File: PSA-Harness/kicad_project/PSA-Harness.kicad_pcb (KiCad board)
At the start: 2 copper layers, 32 x 50 mm, 11 parts, among them J1 to_EPS_1, J2 to_EPS_2, J3 to_ESP_3, J4 to_car_1, J5 to_car_2, J6 to_car_3, J7 USB_C_Receptacle, K1 G6K-2G-Y DC5

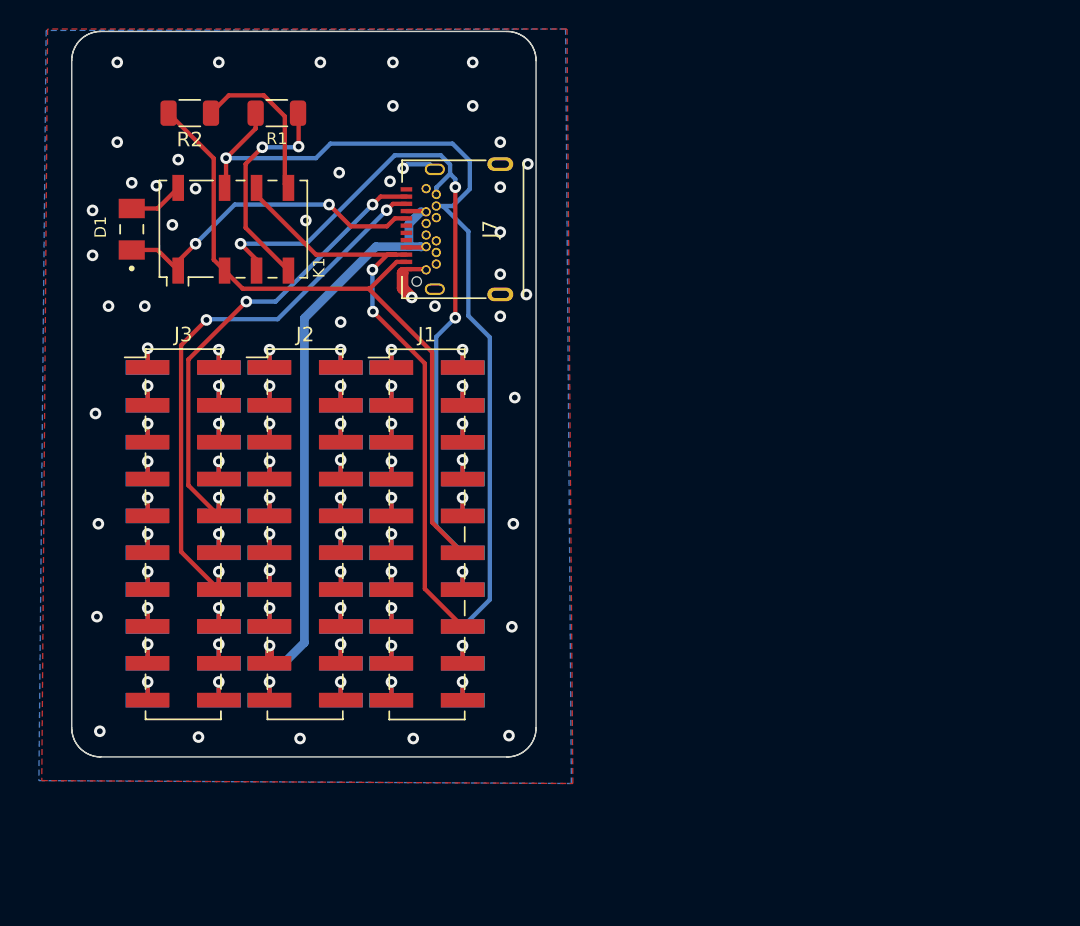
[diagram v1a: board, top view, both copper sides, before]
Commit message: chg: use correct footprints, SMD socket clearence too low
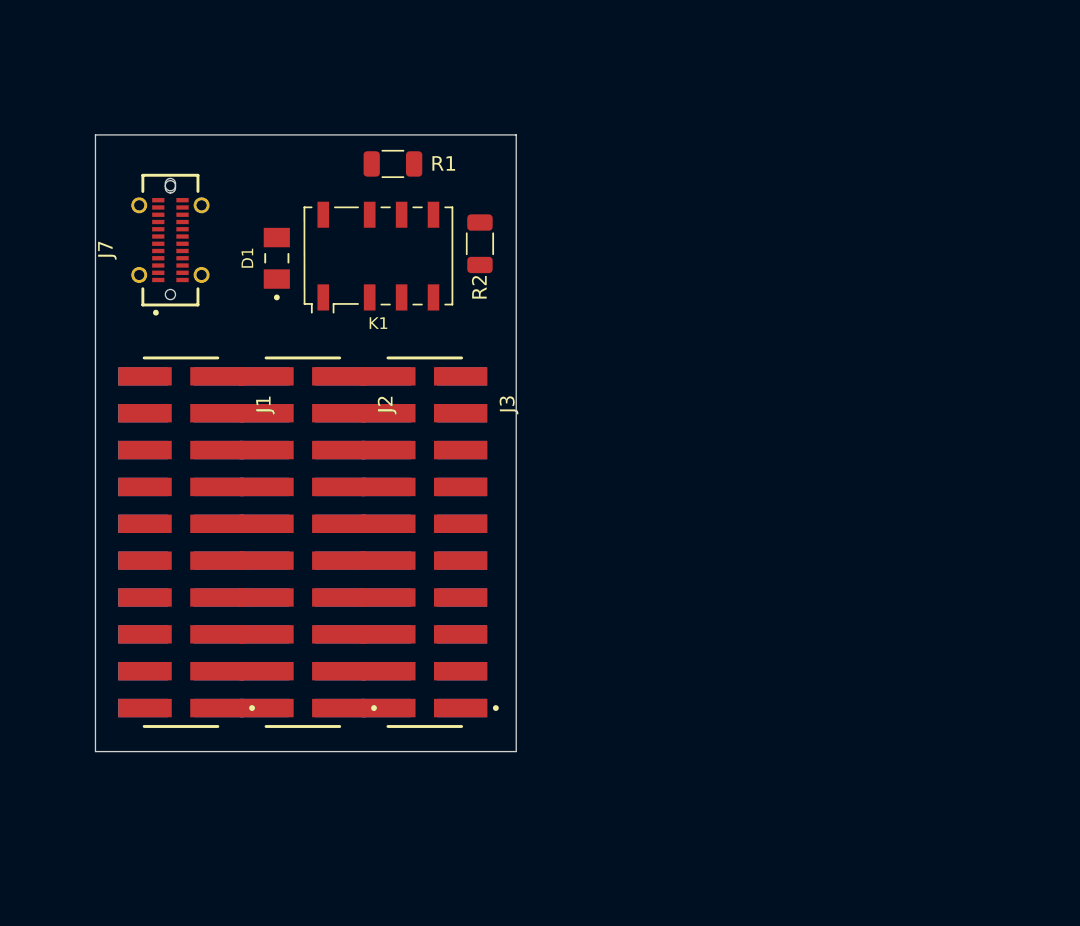
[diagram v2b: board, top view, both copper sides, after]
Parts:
- J1, J2, J3: footprint PSA:PinHeader_2x10_P2.54mm_Vertical_SMD_PSA_small -> PSA:TSM-110-03-X-DV
- J4, J5, J6: footprint PSA:PinSocket_2x10_P2.54mm_Vertical_SMD_PSA -> PSA:SSW-110-22-F-D-VS-K-TR
- J7: footprint PSA:TYPE-C-31-M-04 -> PSA:GCT_USB4115-03-C_REVB4
- moved R2 21.9 mm to (118.0, 101.0), turned to -90 degrees
- moved J7 21.3 mm to (96.7, 100.8)
- moved J4 17.0 mm to (97.4, 121.6), turned to -90 degrees
- moved J1 17.0 mm to (97.4, 121.6), turned to -90 degrees
- moved J3 16.7 mm to (114.2, 121.6), turned to -90 degrees
- moved J6 16.6 mm to (114.2, 121.6), turned to -90 degrees
- moved D1 10.2 mm to (104.0, 102.0)
- moved K1 10.2 mm to (111.0, 101.8)
- moved R1 8.73 mm to (112.0, 95.5)
- moved J5 0.57 mm to (105.8, 121.6), turned to -90 degrees
- moved J2 0.57 mm to (105.8, 121.6), turned to -90 degrees
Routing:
- net CAN2_L: track 59.6 -> 0.00 mm, vias 1 -> 0
- net CAN2_H: track 49.6 -> 0.00 mm, vias 3 -> 0
- net CAN0_H: track 47.1 -> 0.00 mm
- net +12V: track 43.5 -> 0.00 mm, vias 1 -> 0
- net CAN0_L: track 41.7 -> 0.00 mm, vias 2 -> 0
- net CAN1_L: track 40.0 -> 0.00 mm, vias 3 -> 0
- net CAN1_H: track 33.8 -> 0.00 mm, vias 3 -> 0
- net SBU1: track 22.6 -> 0.00 mm, vias 2 -> 0
- net Relay_4: track 15.0 -> 0.00 mm, vias 2 -> 0
- net GND: track 12.1 -> 0.00 mm, vias 43 -> 0
- net Relay_5: track 11.2 -> 0.00 mm
- net 9: track 2.69 -> 0.00 mm, vias 1 -> 0
- net 19: track 2.69 -> 0.00 mm, vias 1 -> 0
- net 59: track 2.68 -> 0.00 mm, vias 1 -> 0
- net 49: track 2.68 -> 0.00 mm, vias 1 -> 0
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- removed copper zone on B.Cu, net GND
- removed copper zone on F.Cu, net GND
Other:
- board size 32 x 50 mm -> 29 x 42.5 mm

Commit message: chg: stacked PCBs
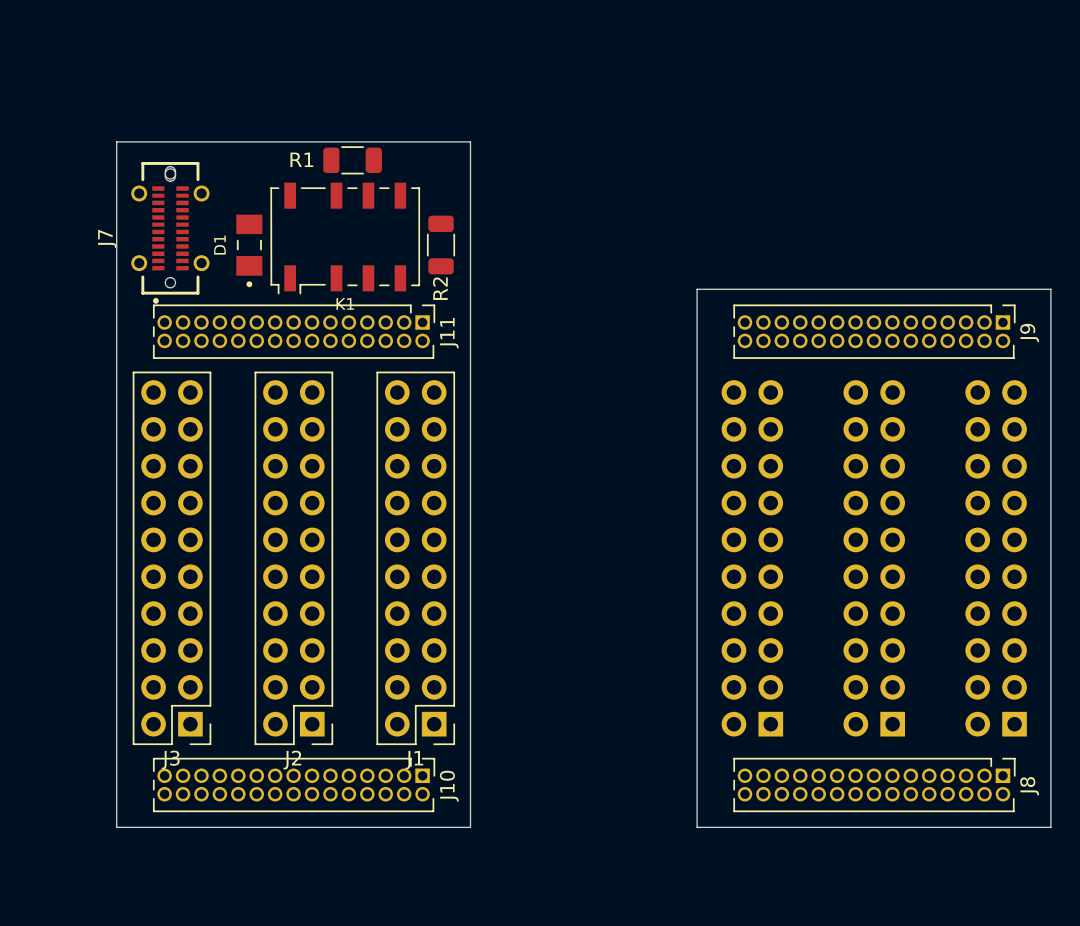
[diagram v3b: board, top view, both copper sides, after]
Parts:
- added J10: B2B_1, Connector_PinHeader_1.27mm:PinHeader_2x15_P1.27mm_Vertical, F.Cu at (114.0, 137.7)
- added J11: B2B_2, Connector_PinHeader_1.27mm:PinHeader_2x15_P1.27mm_Vertical, F.Cu at (114.0, 106.4)
- added J8: B2B_1, Connector_PinHeader_1.27mm:PinHeader_2x15_P1.27mm_Vertical, F.Cu at (154.0, 137.7)
- added J9: B2B_2, Connector_PinHeader_1.27mm:PinHeader_2x15_P1.27mm_Vertical, F.Cu at (154.0, 106.4)
- J1, J2, J3: footprint PSA:TSM-110-03-X-DV -> Connector_PinHeader_2.54mm:PinHeader_2x10_P2.54mm_Vertical
- J4, J5, J6: footprint PSA:SSW-110-22-F-D-VS-K-TR -> Connector_PinSocket_2.54mm:PinSocket_2x10_P2.54mm_Vertical
- moved J4 58.8 mm to (154.8, 134.1), turned to 0 degrees
- moved J5 42.6 mm to (146.4, 134.1), turned to 0 degrees
- moved J6 27.0 mm to (138.0, 134.1), turned to 0 degrees
- moved J1 21.5 mm to (114.8, 134.1), turned to 180 degrees
- moved J3 20.4 mm to (98.0, 134.1), turned to 180 degrees
- moved J2 12.6 mm to (106.4, 134.1), turned to 180 degrees
- moved R1 2.79 mm to (109.2, 95.2), turned to 0 degrees
- moved R2 2.69 mm to (115.3, 101.1)
- moved K1 2.64 mm to (108.7, 100.5)
- moved D1 2.10 mm to (102.1, 101.1)
- moved J7 0.81 mm to (96.7, 99.9)
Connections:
- net Relay_5 renamed Net-(K1-Pad5)
- K1 pad 4: Relay_4 -> Net-(K1-Pad4)
- R1 pad 1: Relay_4 -> CAN2_L
- R1 pad 2: CAN2_L -> Net-(K1-Pad4)
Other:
- board size 29 x 42.5 mm -> 64.4 x 47.2 mm
- board text added: "PCB1"
- board text added: "PCB2"

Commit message: reduce clearances
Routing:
- net +12V: track 0.00 -> 1.73 mm
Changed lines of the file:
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@@
 		)
+	)
+	(segment
+		(start 107.795 119.431603)
+		(end 107.084603 120.142)
+		(width 0.6)
+		(locked yes)
+		(layer "F.Cu")
+		(net 1)
+	)
+	(segment
+		(start 99.151339 101.186)
+		(end 98.426 101.186)
+		(width 0.6)
+		(locked yes)
+		(layer "F.Cu")
+		(net 1)
 	)
 	(embedded_fonts no)

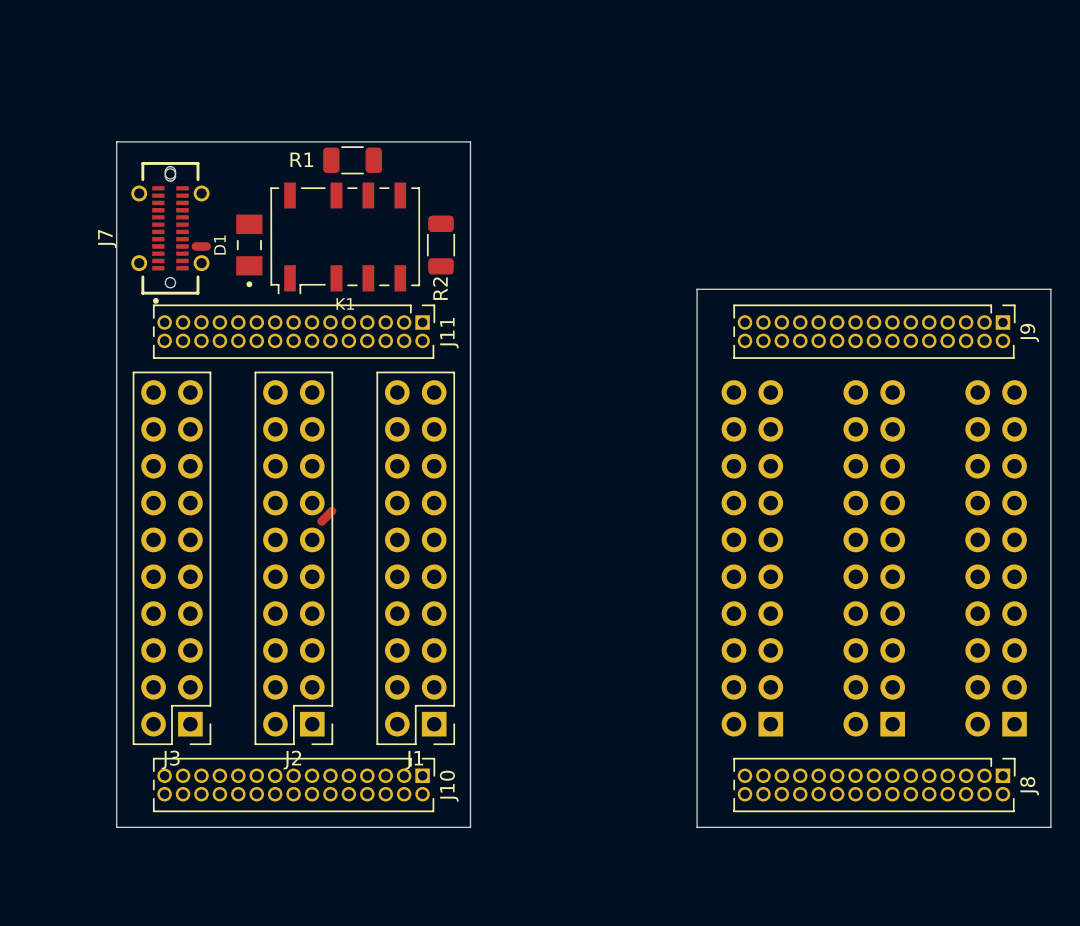
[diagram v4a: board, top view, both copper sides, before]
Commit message: add: connector footprints
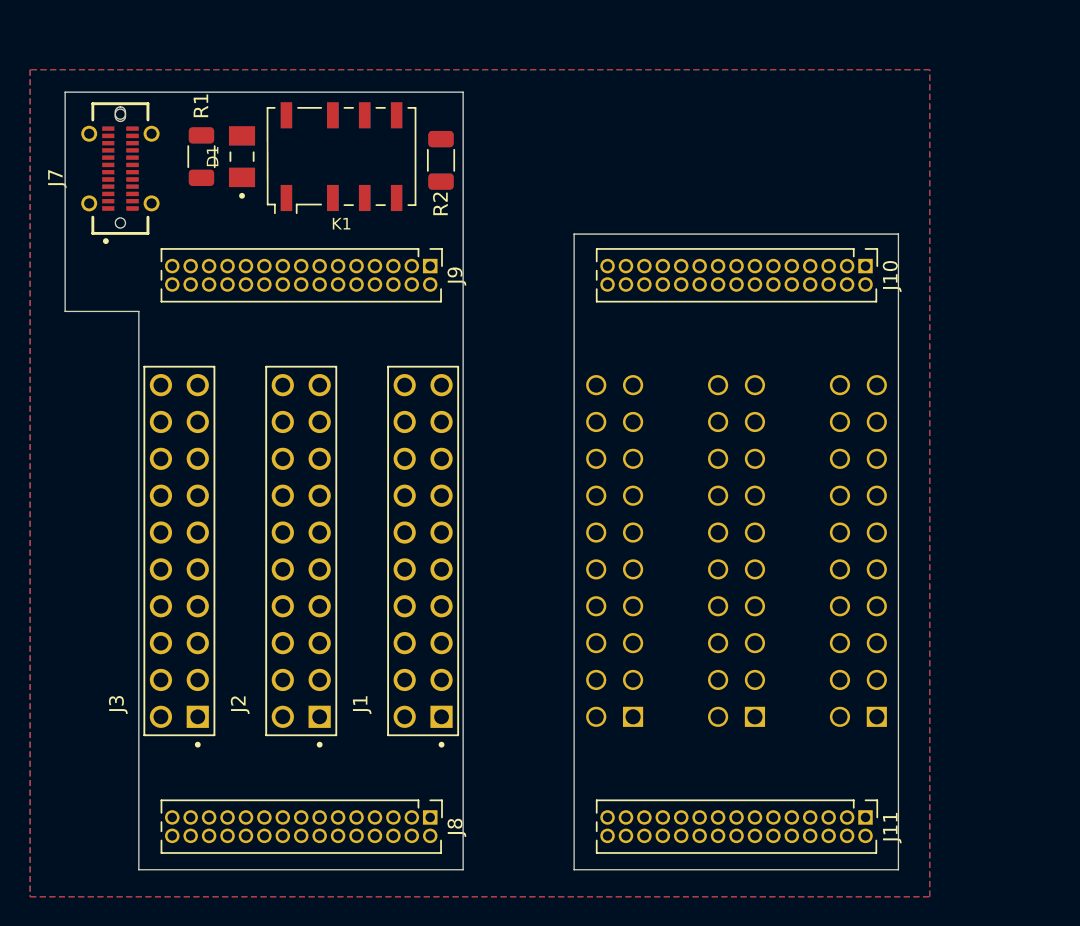
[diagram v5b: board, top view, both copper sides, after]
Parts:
- J1, J2, J3: footprint Connector_PinHeader_2.54mm:PinHeader_2x10_P2.54mm_Vertical -> PSA:10129381-920003BLF
- J4, J5, J6: footprint Connector_PinSocket_2.54mm:PinSocket_2x10_P2.54mm_Vertical -> PSA:ESW-110-44-F-D
- moved J10 46.5 mm to (144.6, 102.5)
- moved J11 45.8 mm to (144.6, 140.5)
- moved J9 39.7 mm to (114.6, 102.5)
- moved J8 39.6 mm to (114.6, 140.5)
- moved J6 16.1 mm to (127.3, 122.2), turned to -90 degrees
- moved J4 16.1 mm to (144.1, 122.2), turned to -90 degrees
- moved J5 16.1 mm to (135.7, 122.2), turned to -90 degrees
- moved J1 12.0 mm to (114.1, 122.2), turned to 90 degrees
- moved J2 12.0 mm to (105.7, 122.2), turned to 90 degrees
- moved J3 12.0 mm to (97.3, 122.2), turned to 90 degrees
- moved R1 10.4 mm to (98.8, 95.0), turned to -90 degrees
- moved D1 6.12 mm to (101.6, 95.0)
- moved R2 5.84 mm to (115.3, 95.2)
- moved K1 5.54 mm to (108.5, 95.0)
- moved J7 5.37 mm to (93.2, 95.8)
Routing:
- net +12V: track 1.73 -> 0.00 mm
- added copper zone on B.Cu, net GND
- added copper zone on F.Cu, net GND
- added copper zone on In1.Cu, net GND
- added copper zone on In2.Cu, net GND
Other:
- board size 64.4 x 47.2 mm -> 57.4 x 53.6 mm
- copper layers 2 -> 4

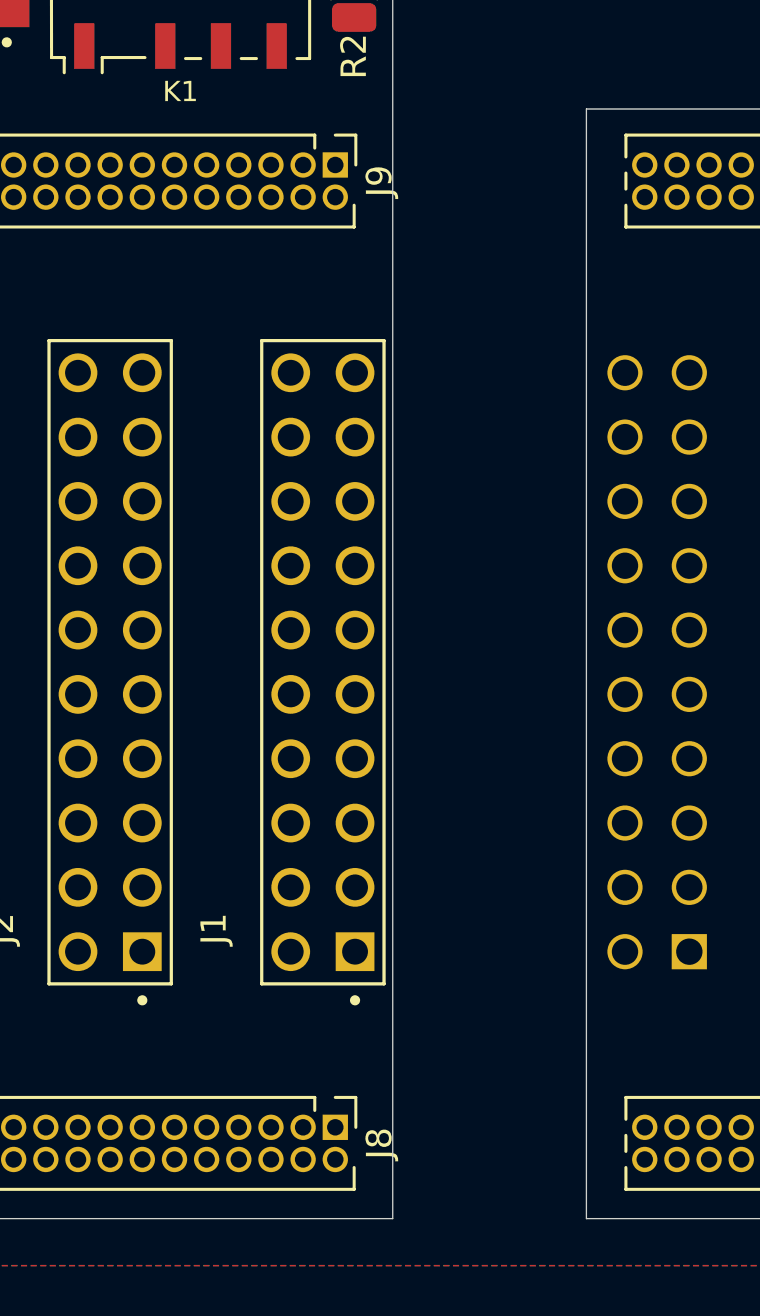
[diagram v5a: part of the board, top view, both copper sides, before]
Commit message: chg: rearrange pcb interconnect pins
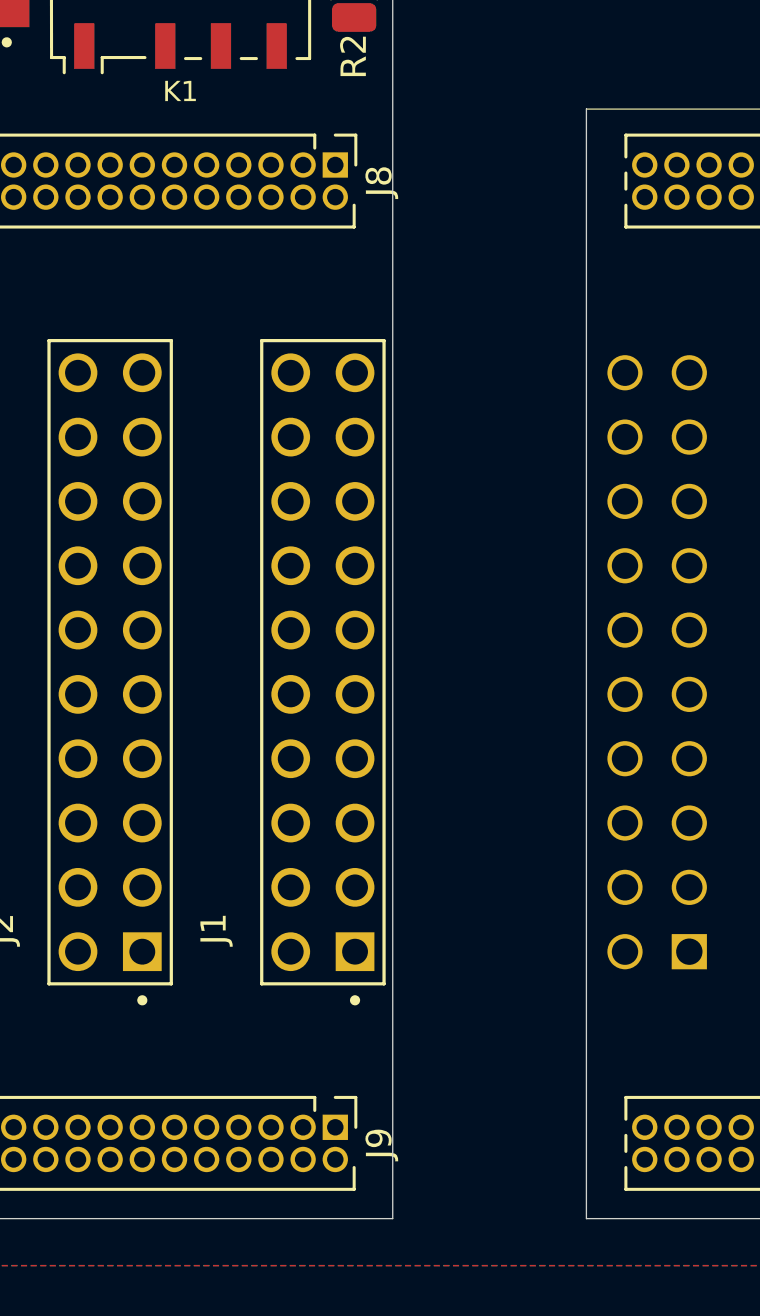
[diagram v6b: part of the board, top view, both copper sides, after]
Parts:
- moved J8 38.0 mm to (114.6, 102.5)
- moved J9 38.0 mm to (114.6, 140.5)
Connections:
- J10 pad 1: 1 -> 11
- J10 pad 10: 10 -> 16
- J10 pad 11: 11 -> 6
- J10 pad 12: 12 -> 17
- J10 pad 13: 13 -> 4
- J10 pad 14: 14 -> 18
- J10 pad 15: 15 -> 2
- J10 pad 16: 16 -> 19
- J10 pad 17: 17 -> 1
- J10 pad 18: 18 -> 20
- J10 pad 19: 19 -> CAN2_H
- J10 pad 2: 2 -> 12
- J10 pad 20: 20 -> 21
- J10 pad 21: 21 -> CAN2_L
- J10 pad 23: 23 -> CAN1_H
- J10 pad 24: GND -> 23
- J10 pad 25: 25 -> CAN1_L
- J10 pad 26: 26 -> 25
- J10 pad 27: 27 -> GND
- J10 pad 28: 28 -> 26
- J10 pad 29: 29 -> +12V
- J10 pad 3: CAN2_L -> 10
- J10 pad 30: 30 -> 27
- J10 pad 4: 4 -> 13
- J10 pad 5: CAN2_H -> 9
- J10 pad 6: 6 -> 14
- J10 pad 7: 7 -> 8
- J10 pad 8: 8 -> 15
- J10 pad 9: 9 -> 7
- J11 pad 1: 31 -> 43
- J11 pad 10: 40 -> 50
- J11 pad 11: 41 -> 38
- J11 pad 12: 42 -> 51
- J11 pad 13: 43 -> 37
- J11 pad 14: CAN1_L -> 52
- J11 pad 15: 45 -> 36
- J11 pad 16: CAN1_H -> 53
- J11 pad 17: 47 -> 35
- J11 pad 18: 48 -> 54
- J11 pad 19: 49 -> 34
- J11 pad 2: +12V -> 45
- J11 pad 20: 50 -> 55
- J11 pad 21: 51 -> 33
- J11 pad 22: 52 -> 56
- J11 pad 23: 53 -> 31
- J11 pad 24: 54 -> 57
- J11 pad 25: 55 -> 30
- J11 pad 26: 56 -> 58
- J11 pad 27: 57 -> 29
- J11 pad 28: 58 -> 59
- J11 pad 29: 59 -> 28
- J11 pad 3: 33 -> 42
- J11 pad 4: 34 -> 47
- J11 pad 5: 35 -> 41
- J11 pad 6: 36 -> 48
- J11 pad 7: 37 -> 40
- J11 pad 8: 38 -> 49
- J8 pad 1: 1 -> 11
- J8 pad 10: 10 -> 16
- J8 pad 11: 11 -> 6
- J8 pad 12: 12 -> 17
- J8 pad 13: 13 -> 4
- J8 pad 14: 14 -> 18
- J8 pad 15: 15 -> 2
- J8 pad 16: 16 -> 19
- J8 pad 17: 17 -> 1
- J8 pad 18: 18 -> 20
- J8 pad 19: 19 -> CAN2_H
- J8 pad 2: 2 -> 12
- J8 pad 20: 20 -> 21
- J8 pad 21: 21 -> CAN2_L
- J8 pad 23: 23 -> CAN1_H
- J8 pad 24: GND -> 23
- J8 pad 25: 25 -> CAN1_L
- J8 pad 26: 26 -> 25
- J8 pad 27: 27 -> GND
- J8 pad 28: 28 -> 26
- J8 pad 29: 29 -> +12V
- J8 pad 3: CAN2_L -> 10
- J8 pad 30: 30 -> 27
- J8 pad 4: 4 -> 13
- J8 pad 5: CAN2_H -> 9
- J8 pad 6: 6 -> 14
- J8 pad 7: 7 -> 8
- J8 pad 8: 8 -> 15
- J8 pad 9: 9 -> 7
- J9 pad 1: 31 -> 43
- J9 pad 10: 40 -> 50
- J9 pad 11: 41 -> 38
- J9 pad 12: 42 -> 51
- J9 pad 13: 43 -> 37
- J9 pad 14: CAN1_L -> 52
- J9 pad 15: 45 -> 36
- J9 pad 16: CAN1_H -> 53
- J9 pad 17: 47 -> 35
- J9 pad 18: 48 -> 54
- J9 pad 19: 49 -> 34
- J9 pad 2: +12V -> 45
- J9 pad 20: 50 -> 55
- J9 pad 21: 51 -> 33
- J9 pad 22: 52 -> 56
- J9 pad 23: 53 -> 31
- J9 pad 24: 54 -> 57
- J9 pad 25: 55 -> 30
- J9 pad 26: 56 -> 58
- J9 pad 27: 57 -> 29
- J9 pad 28: 58 -> 59
- J9 pad 29: 59 -> 28
- J9 pad 3: 33 -> 42
- J9 pad 4: 34 -> 47
- J9 pad 5: 35 -> 41
- J9 pad 6: 36 -> 48
- J9 pad 7: 37 -> 40
- J9 pad 8: 38 -> 49
